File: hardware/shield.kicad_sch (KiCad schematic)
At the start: 12 parts, among them P10 CONN_01X01, P11 CONN_01X01, P12 CONN_01X01, P2 Power, P3 Analog, P5 GPIO, P6 GPIO, P7 GPIO, P8 CONN_01X01, P9 CONN_01X01

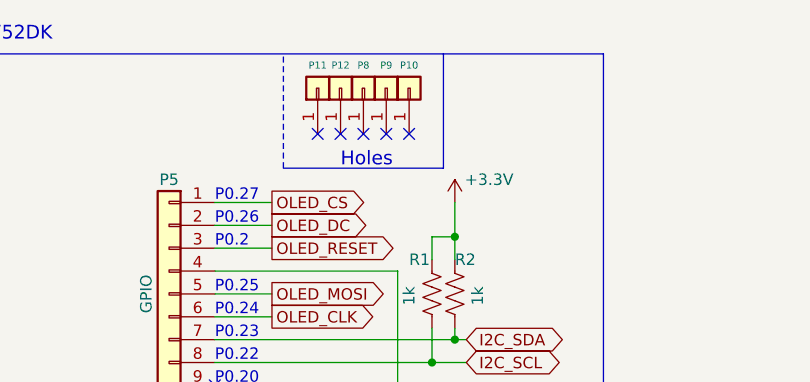
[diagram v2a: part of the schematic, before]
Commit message: Re-align schematic to PCB
While laying out the PCB, I modified the footprints used for the
headers connecting to the nRF52-DK and changed some of the header value
names. This commit makes the same updates to the schematic sheets.
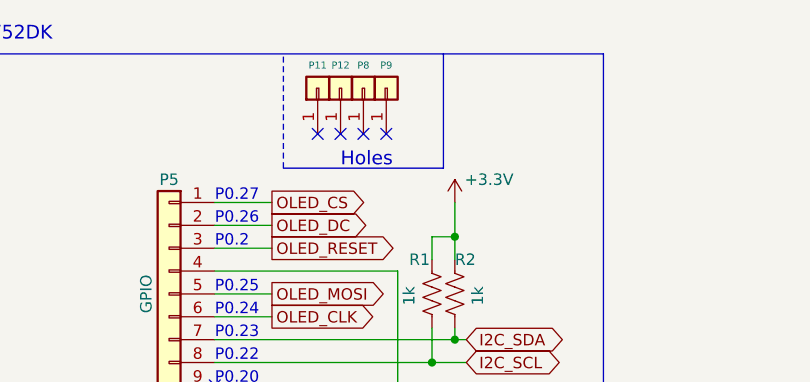
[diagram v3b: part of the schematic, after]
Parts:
- removed P10: CONN_01X01, Socket_Arduino_Mega:Arduino_1pin, symbol Connector_Generic:Conn_01x01
- P2, P6: footprint Socket_Arduino_Mega:Socket_Strip_Arduino_1x08 -> Connector_PinHeader_2.54mm:PinHeader_1x08_P2.54mm_Vertical
- P5: footprint Socket_Arduino_Mega:Socket_Strip_Arduino_1x10 -> Connector_PinHeader_2.54mm:PinHeader_1x10_P2.54mm_Vertical
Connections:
- no-connect marks 12 -> 11
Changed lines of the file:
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@@
   (no_connect (at 156.21 38.1))
   (no_connect (at 161.29 38.1))
-  (no_connect (at 163.83 38.1))
   (no_connect (at 109.22 68.58))
   (no_connect (at 158.75 38.1))
@@
     (pin "1")
   )
-  (symbol (lib_id "Connector_Generic:Conn_01x01") (at 163.83 33.02 90) (unit 1)
-    (in_bom yes) (on_board yes)
-    (property "Reference" "P10" (id 0) (at 163.83 30.48 90)
-      (effects (font (size 0.7874 0.7874)))
-    )
-    (property "Value" "CONN_01X01" (id 1) (at 163.83 30.48 90)
-      (effects (font (size 1.27 1.27)) hide)
-    )
-    (property "Footprint" "Socket_Arduino_Mega:Arduino_1pin" (id 2) (at 163.83 33.02 0)
-      (effects (font (size 1.27 1.27)) hide)
-    )
-    (property "Datasheet" "" (id 3) (at 163.83 33.02 0))
-    (pin "1")
-  )
   (symbol (lib_id "Connector_Generic:Conn_01x08") (at 114.3 58.42 0) (unit 1)
     (in_bom yes) (on_board yes)
     (property "Reference" "P2" (id 0) (at 114.3 48.26 0))
     (property "Value" "Power" (id 1) (at 116.84 58.42 90))
-    (property "Footprint" "Socket_Arduino_Mega:Socket_Strip_Arduino_1x08" (id 2) (at 114.3 58.42 0)
+    (property "Footprint" "Connector_PinHeader_2.54mm:PinHeader_1x08_P2.54mm_Vertical" (id 2) (at 114.3 58.42 0)
       (effects (font (size 1.27 1.27)) hide)
     )
@@
     (property "Reference" "P5" (id 0) (at 137.16 43.18 0))
     (property "Value" "GPIO" (id 1) (at 134.62 55.88 90))
-    (property "Footprint" "Socket_Arduino_Mega:Socket_Strip_Arduino_1x10" (id 2) (at 137.16 55.88 0)
+    (property "Footprint" "Connector_PinHeader_2.54mm:PinHeader_1x10_P2.54mm_Vertical" (id 2) (at 137.16 55.88 0)
       (effects (font (size 1.27 1.27)) hide)
     )
@@
     (property "Reference" "P6" (id 0) (at 137.16 76.2 0))
     (property "Value" "GPIO" (id 1) (at 134.62 86.36 90))
-    (property "Footprint" "Socket_Arduino_Mega:Socket_Strip_Arduino_1x08" (id 2) (at 137.16 86.36 0)
+    (property "Footprint" "Connector_PinHeader_2.54mm:PinHeader_1x08_P2.54mm_Vertical" (id 2) (at 137.16 86.36 0)
       (effects (font (size 1.27 1.27)) hide)
     )
@@
     )
     (path "/fa8f6b07-7d40-4224-a9dc-a3ae06b76dce/c41f1f65-4d05-4264-a854-9f96f99e463e"
-      (reference "J5") (unit 1) (value "Left Photo Cell") (footprint "Connector_PinSocket_2.54mm:PinSocket_1x02_P2.54mm_Vertical")
+      (reference "J5") (unit 1) (value "Left Photo") (footprint "Connector_PinSocket_2.54mm:PinSocket_1x02_P2.54mm_Vertical")
     )
     (path "/fa8f6b07-7d40-4224-a9dc-a3ae06b76dce/8dd47c44-d93d-44e4-bfe0-d5568149451f"
-      (reference "J6") (unit 1) (value "Front Left Distance Sensor") (footprint "Connector_PinSocket_2.54mm:PinSocket_1x07_P2.54mm_Vertical")
+      (reference "J6") (unit 1) (value "Front Left Distance") (footprint "Connector_PinSocket_2.54mm:PinSocket_1x07_P2.54mm_Vertical")
     )
     (path "/fa8f6b07-7d40-4224-a9dc-a3ae06b76dce/241435af-54e9-4685-b37a-3161a8718ba3"
-      (reference "J7") (unit 1) (value "Back Left Distance Sensor") (footprint "Connector_PinSocket_2.54mm:PinSocket_1x07_P2.54mm_Vertical")
+      (reference "J7") (unit 1) (value "Back Left Distance") (footprint "Connector_PinSocket_2.54mm:PinSocket_1x07_P2.54mm_Vertical")
     )
     (path "/fa8f6b07-7d40-4224-a9dc-a3ae06b76dce/1a78194f-66b2-4f54-beb3-01fb20a69781"
@@
     )
     (path "/fa8f6b07-7d40-4224-a9dc-a3ae06b76dce/b9d391e5-c004-47c7-88fb-f10dbe91d248"
-      (reference "J11") (unit 1) (value "Front Center Distance Sensor") (footprint "Connector_PinSocket_2.54mm:PinSocket_1x07_P2.54mm_Vertical")
+      (reference "J11") (unit 1) (value "Front Center Distance") (footprint "Connector_PinSocket_2.54mm:PinSocket_1x07_P2.54mm_Vertical")
     )
     (path "/fa8f6b07-7d40-4224-a9dc-a3ae06b76dce/94517954-83cb-4fc7-9baa-5ebc7d4b74eb"
-      (reference "J13") (unit 1) (value "Bumper Switch 1") (footprint "Connector_PinSocket_2.54mm:PinSocket_1x02_P2.54mm_Horizontal")
+      (reference "J13") (unit 1) (value "Bump1") (footprint "Connector_PinSocket_2.54mm:PinSocket_1x02_P2.54mm_Horizontal")
     )
     (path "/fa8f6b07-7d40-4224-a9dc-a3ae06b76dce/72556355-70a9-4b7d-b310-0fb788bbf3c7"
-      (reference "J14") (unit 1) (value "Bumper Switch 2") (footprint "Connector_PinSocket_2.54mm:PinSocket_1x02_P2.54mm_Horizontal")
+      (reference "J14") (unit 1) (value "Bump2") (footprint "Connector_PinSocket_2.54mm:PinSocket_1x02_P2.54mm_Horizontal")
     )
     (path "/fa8f6b07-7d40-4224-a9dc-a3ae06b76dce/1d294281-1e4b-49e0-aceb-f1ea3f848d1d"
-      (reference "J15") (unit 1) (value "Bumper Switch 3") (footprint "Connector_PinSocket_2.54mm:PinSocket_1x02_P2.54mm_Horizontal")
+      (reference "J15") (unit 1) (value "Bump3") (footprint "Connector_PinSocket_2.54mm:PinSocket_1x02_P2.54mm_Horizontal")
     )
     (path "/fa8f6b07-7d40-4224-a9dc-a3ae06b76dce/d3051d8f-5266-489d-9e3d-0145522584e5"
-      (reference "J16") (unit 1) (value "PIR Sensor") (footprint "Connector_PinSocket_2.54mm:PinSocket_1x03_P2.54mm_Vertical")
+      (reference "J16") (unit 1) (value "PIR") (footprint "Connector_PinSocket_2.54mm:PinSocket_1x03_P2.54mm_Vertical")
     )
     (path "/fa8f6b07-7d40-4224-a9dc-a3ae06b76dce/02f1e5e4-55a6-4970-ac87-9fdf8bcf971f"
-      (reference "J17") (unit 1) (value "Front Right Distance Sensor") (footprint "Connector_PinSocket_2.54mm:PinSocket_1x07_P2.54mm_Vertical")
+      (reference "J17") (unit 1) (value "Front Right Distance") (footprint "Connector_PinSocket_2.54mm:PinSocket_1x07_P2.54mm_Vertical")
     )
     (path "/fa8f6b07-7d40-4224-a9dc-a3ae06b76dce/80ce8885-4772-497b-b446-6f54fda8d63e"
-      (reference "J18") (unit 1) (value "Back Right Distance Sensor") (footprint "Connector_PinSocket_2.54mm:PinSocket_1x07_P2.54mm_Vertical")
+      (reference "J18") (unit 1) (value "Back Right Distance") (footprint "Connector_PinSocket_2.54mm:PinSocket_1x07_P2.54mm_Vertical")
     )
     (path "/fa8f6b07-7d40-4224-a9dc-a3ae06b76dce/a014ebbd-2c2d-471f-a9ea-21ecea81ec81"
-      (reference "J19") (unit 1) (value "Left Cliff Sensor") (footprint "Connector_PinSocket_2.54mm:PinSocket_1x07_P2.54mm_Horizontal")
+      (reference "J19") (unit 1) (value "Left Cliff") (footprint "Connector_PinSocket_2.54mm:PinSocket_1x07_P2.54mm_Horizontal")
     )
     (path "/fa8f6b07-7d40-4224-a9dc-a3ae06b76dce/cbbf99b0-f621-4255-9478-f224af720ca8"
-      (reference "J20") (unit 1) (value "Right Cliff Sensor") (footprint "Connector_PinSocket_2.54mm:PinSocket_1x07_P2.54mm_Horizontal")
+      (reference "J20") (unit 1) (value "Right Cliff") (footprint "Connector_PinSocket_2.54mm:PinSocket_1x07_P2.54mm_Horizontal")
     )
     (path "/fa8f6b07-7d40-4224-a9dc-a3ae06b76dce/84375f8b-a254-4cdf-a053-6e6c22a58f9b"
@@
     )
     (path "/2bb6c136-8f3a-4530-8b08-9c3c632d4195/7385c06f-c56f-4edf-843c-21a50d007fa2"
-      (reference "J26") (unit 1) (value "LeftMotor Conn") (footprint "Connector_PinSocket_2.54mm:PinSocket_1x06_P2.54mm_Horizontal")
+      (reference "J26") (unit 1) (value "Left Motor") (footprint "Connector_PinSocket_2.54mm:PinSocket_1x06_P2.54mm_Horizontal")
     )
     (path "/2bb6c136-8f3a-4530-8b08-9c3c632d4195/2f3ca387-0a81-462f-a184-dfe2120fe907"
-      (reference "J27") (unit 1) (value "RightMotor Conn") (footprint "Connector_PinSocket_2.54mm:PinSocket_1x06_P2.54mm_Horizontal")
+      (reference "J27") (unit 1) (value "Right Motor") (footprint "Connector_PinSocket_2.54mm:PinSocket_1x06_P2.54mm_Horizontal")
     )
     (path "/00000000-0000-0000-0000-000056d71773"
-      (reference "P2") (unit 1) (value "Power") (footprint "Socket_Arduino_Mega:Socket_Strip_Arduino_1x08")
+      (reference "P2") (unit 1) (value "Power") (footprint "Connector_PinHeader_2.54mm:PinHeader_1x08_P2.54mm_Vertical")
     )
     (path "/00000000-0000-0000-0000-000056d72f1c"
@@
     )
     (path "/00000000-0000-0000-0000-000056d72368"
-      (reference "P5") (unit 1) (value "GPIO") (footprint "Socket_Arduino_Mega:Socket_Strip_Arduino_1x10")
+      (reference "P5") (unit 1) (value "GPIO") (footprint "Connector_PinHeader_2.54mm:PinHeader_1x10_P2.54mm_Vertical")
     )
     (path "/00000000-0000-0000-0000-000056d734d0"
-      (reference "P6") (unit 1) (value "GPIO") (footprint "Socket_Arduino_Mega:Socket_Strip_Arduino_1x08")
+      (reference "P6") (unit 1) (value "GPIO") (footprint "Connector_PinHeader_2.54mm:PinHeader_1x08_P2.54mm_Vertical")
     )
     (path "/00000000-0000-0000-0000-000056d73f2c"
@@
       (reference "P9") (unit 1) (value "CONN_01X01") (footprint "Socket_Arduino_Mega:Arduino_1pin")
     )
-    (path "/00000000-0000-0000-0000-000056d711a2"
-      (reference "P10") (unit 1) (value "CONN_01X01") (footprint "Socket_Arduino_Mega:Arduino_1pin")
-    )
     (path "/00000000-0000-0000-0000-000056d70b71"
